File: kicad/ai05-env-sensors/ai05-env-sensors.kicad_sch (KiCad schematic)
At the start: 1 part, among them CN1 Leafony Bus

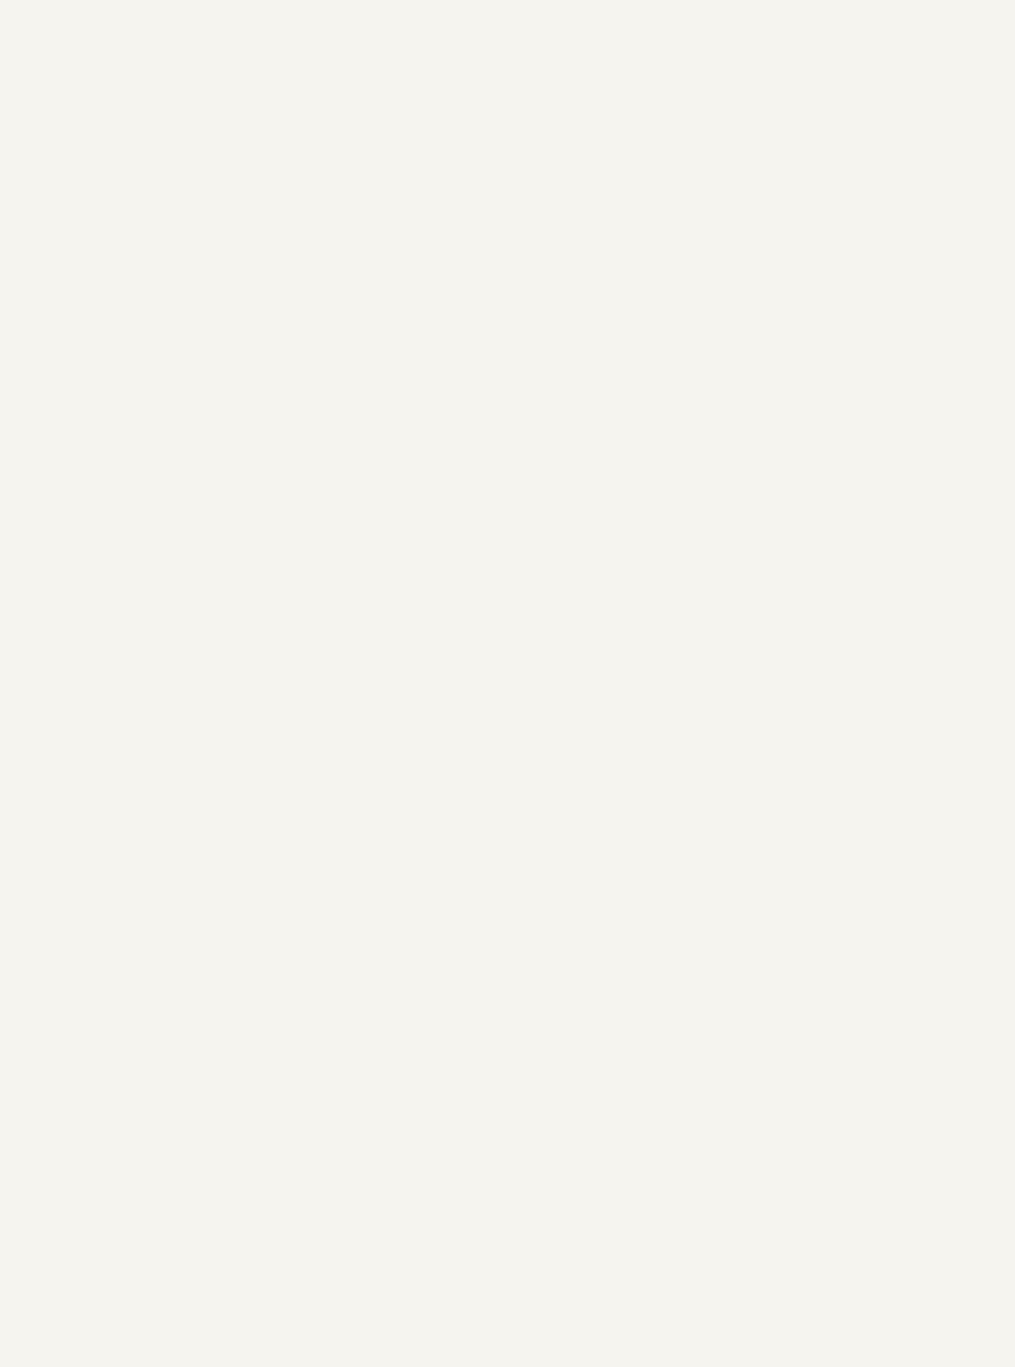
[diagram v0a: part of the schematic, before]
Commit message: Add new footprints for various sensors and connectors
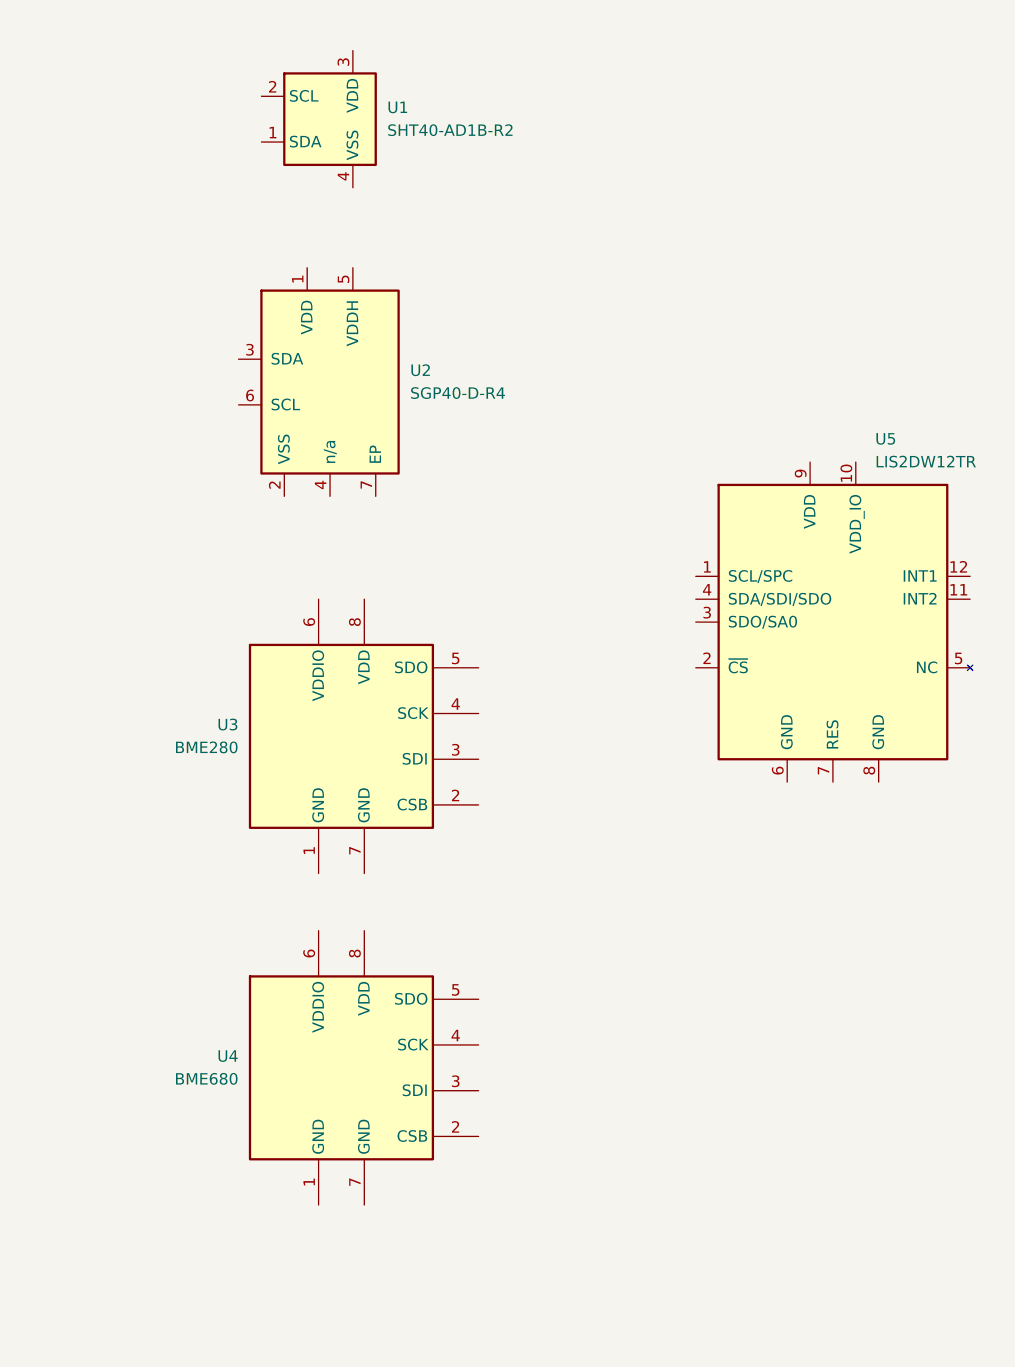
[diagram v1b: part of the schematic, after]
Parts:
- added U1: SHT40-AD1B-R2, AI05:Sensirion_DFN-4_1.5x1.5mm_P0.8mm_SHT4x_NoCentralPad, symbol AI05:SHT40-AD1B-R2
- added U2: SGP40-D-R4, AI05:Sensirion_DFN-6-1EP_2.44x2.44mm_P0.8mm_SGP40, symbol AI05:SGP40-D-R4
- added U3: BME280, AI05:Bosch_LGA-8_2.5x2.5mm_P0.65mm_ClockwisePinNumbering, symbol AI05:BME280
- added U4: BME680, AI05:Bosch_LGA-8_3x3mm_P0.8mm_ClockwisePinNumbering_Recommended, symbol AI05:BME680
- added U5: LIS2DW12TR, AI05:LGA-12_2x2mm_P0.5mm, symbol AI05:LIS2DW12TR

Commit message: レイアウト完成
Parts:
- added C2, C3: 1u(M)/10V/X5R, Capacitor_SMD:C_0402_1005Metric, symbol Device:C_Small
- added C20, C21, C22, C23, C24, C25, C26: 0.1u(K)/50V/X7R, Capacitor_SMD:C_0402_1005Metric, symbol Device:C_Small
- added C27: 10u(M)/35V/X5R, Capacitor_SMD:C_0603_1608Metric, symbol Device:C_Small
- added J1: Conn_01x04_Pin, AI05:PinHeader_1x04_P2.54mm_Horizontal, symbol Connector:Conn_01x04_Pin
- added R10: 4.7Ω(J), Resistor_SMD:R_0402_1005Metric, symbol Device:R_Small
- added R18, R19: 2.7kΩ(J), Resistor_SMD:R_0402_1005Metric, symbol Device:R_Small
- CN1: now left out of the parts list
- U1, U2, U4: now not fitted
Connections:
- net +3V3: now also U1.3 (VDD), U2.5 (VDDH), U3.2 (CSB), U3.6 (VDDIO), U3.8 (VDD), U4.2 (CSB), U4.6 (VDDIO), U4.8 (VDD), U5.10 (VDD_IO), U5.2 (~{CS}), U5.9 (VDD), C2.1, C20.2, C21.2, C22.2, C23.2, C24.2, C25.2, C26.2, C27.1, J1.2 (Pin_2), R10.2, R18.1, R19.1
- net D3: now also U5.12 (INT1)
- net GND: now also U1.4 (VSS), U2.2 (VSS), U2.4 (n/a), U2.7 (EP), U3.1 (GND), U3.5 (SDO), U3.7 (GND), U4.1 (GND), U4.5 (SDO), U4.7 (GND), U5.3 (SDO/SA0), U5.6 (GND), U5.7 (RES), U5.8 (GND), C2.2, C20.1, C21.1, C22.1, C23.1, C24.1, C25.1, C26.1, C27.2, C3.1, J1.1 (Pin_1)
- net SCL: now also U1.2 (SCL), U2.6 (SCL), U3.4 (SCK), U4.4 (SCK), U5.1 (SCL/SPC), J1.4 (Pin_4), R18.2
- net SDA: now also U1.1 (SDA), U2.3 (SDA), U3.3 (SDI), U4.3 (SDI), U5.4 (SDA/SDI/SDO), J1.3 (Pin_3), R19.2
- net at U2.1 (VDD): now also C3.2, R10.1
- no-connect marks 0 -> 1
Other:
- moved on the sheet: U3, U5
